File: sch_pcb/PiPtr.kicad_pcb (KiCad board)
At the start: 4 copper layers, 101.6 x 141.7 mm, 388 parts, among them J101 GLOBAL_LINK_LEFT, J102 GLOBAL_LINK_RIGHT, J107 RASPBERRY_PI, J111 FP_PIXEL, J112 AM2302, J204 DE9F, J305 AUX_IO_1, J307 SPARE, J308 AUX_IO_2, J311 I2C1_5V, J312 RTC, J315 OLED_SSD1306, J404 DE9F, J501 MicroUSB, P301 Chassis, Q101 BSS138, Q102 BSS138, Q103 BSS138, Q104 BSS138, Q105 BSS138, Q201 BSS138, Q202 BSS138, Q203 BSS138, Q401 BSS138, Q402 BSS138, Q403 BSS138, Q501 NX2301P,215, U101 MCP23008, U102 IP4234CZ6, U103 MCP4351, U104 74HCT138, U105 74LV1T125, U106 MCP6004T, U107 MCP4351, U108 74LVC4066, U109 74LVC1G3157, U110 74LV1T125, U111 74LV1T125, U112 74LV1T125, U113 74LV1T125, U201 MCP6004T, U202 74LVC1G3157, U203 74LVC1G3157, U204 74LVC4066, U205 MCP6004T, U206 74LVC1G3157, U207 MCP6S26, U208 MCP23008, U301 MCP23017, U304 MCP3008, U305 MCP1703A-2502/MB, U306 TPS54302, U307 IP4234CZ6, U308 IP4234CZ6, U401 MCP6004T, U402 74LVC1G3157, U403 74LVC1G3157, U404 74LVC4066, U405 MCP6004T, U406 74LVC1G3157, U407 MCP6S26, U408 MCP23008, U501 CM108B, U502 CM108B, U503 TUSB2036, U504 MCP1703A-3302/MB, U505 CM108B, Y501 6MHz

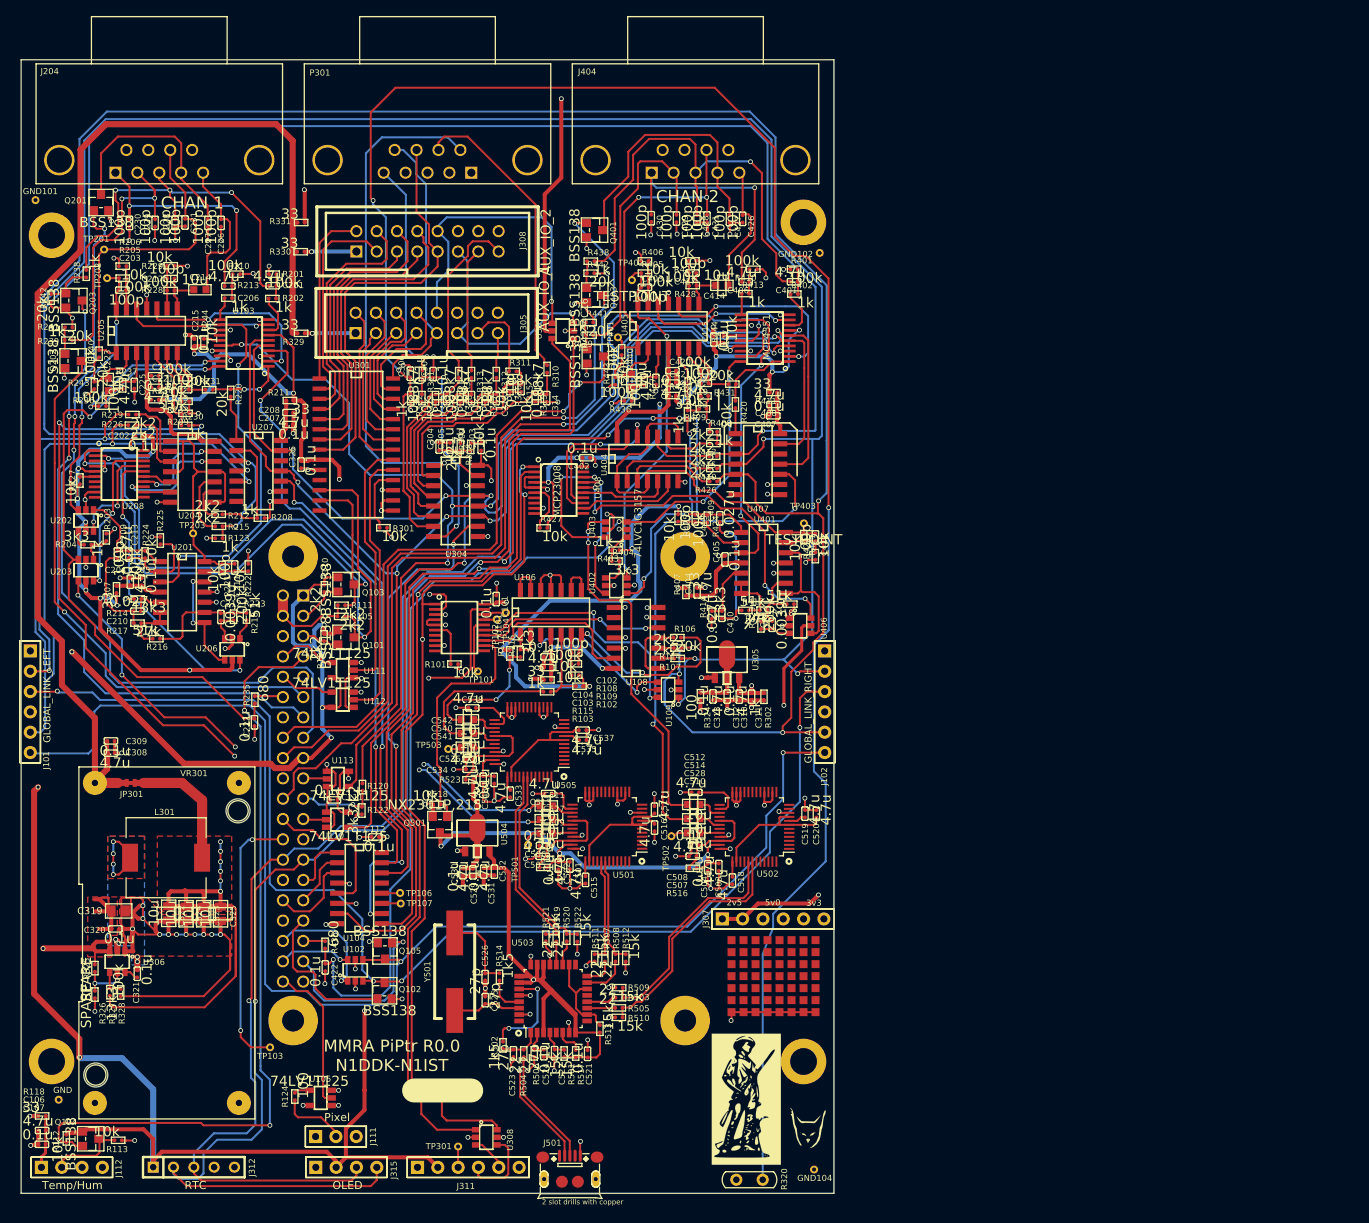
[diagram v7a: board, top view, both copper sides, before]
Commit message: Version with updated silkscreen
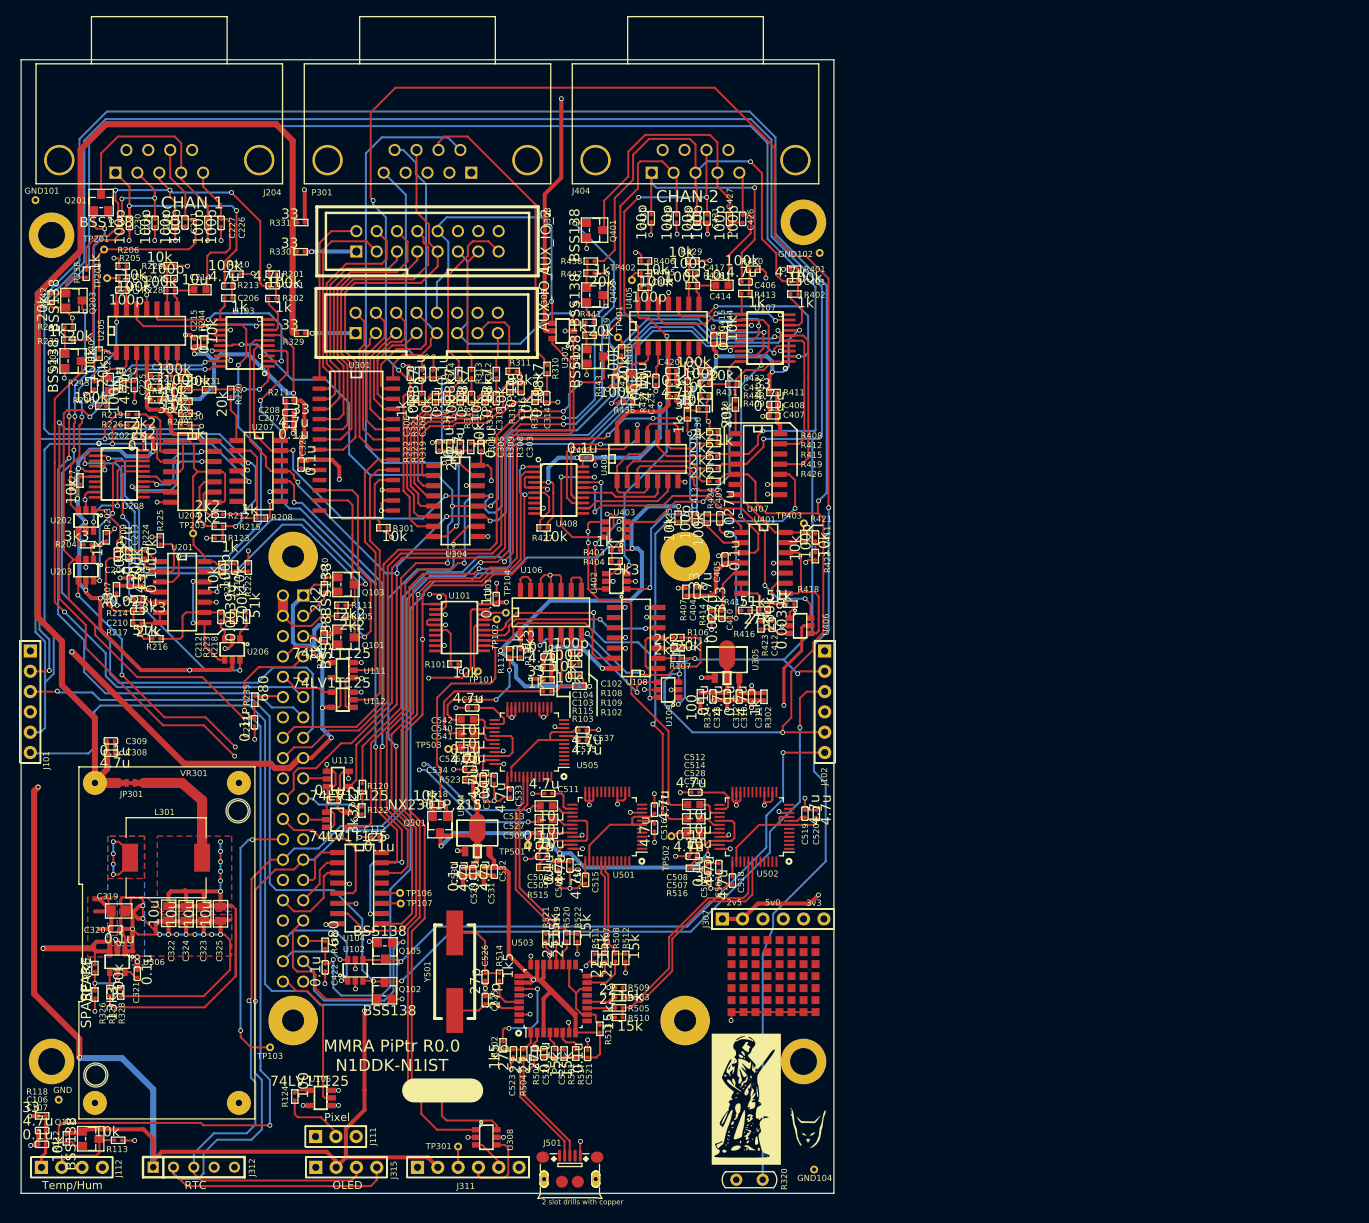
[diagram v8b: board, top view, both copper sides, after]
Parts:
- moved U402 0.53 mm to (131.6, 93.1)
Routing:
- net +12V: track 243.9 -> 239.9 mm
- net Net-(R404-Pad2): track 3.44 -> 2.76 mm
